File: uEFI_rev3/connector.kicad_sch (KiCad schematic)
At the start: 23 parts, among them J3 36638-0002, Q10 IRF540N, Q5 SS8050, Q6 IRF540N, Q7 IRF540N, U4 MIC2940A-3.3WU, U5 MIC2940A-5.0WT, U6 LT4363IMS

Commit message: rev3, jtag
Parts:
- U6: footprint Package_SO:SOIC-16W_7.5x10.3mm_P1.27mm -> Package_SO:MSOP-12_3x4mm_P0.65mm
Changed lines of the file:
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@@
     (property "Reference" "U6" (id 0) (at 101.6 105.029 0))
     (property "Value" "LT4363IMS" (id 1) (at 101.6 107.3404 0))
-    (property "Footprint" "Package_SO:SOIC-16W_7.5x10.3mm_P1.27mm" (id 2) (at 101.6 113.03 0)
+    (property "Footprint" "Package_SO:MSOP-12_3x4mm_P0.65mm" (id 2) (at 101.6 113.03 0)
       (effects (font (size 1.27 1.27)) hide)
     )

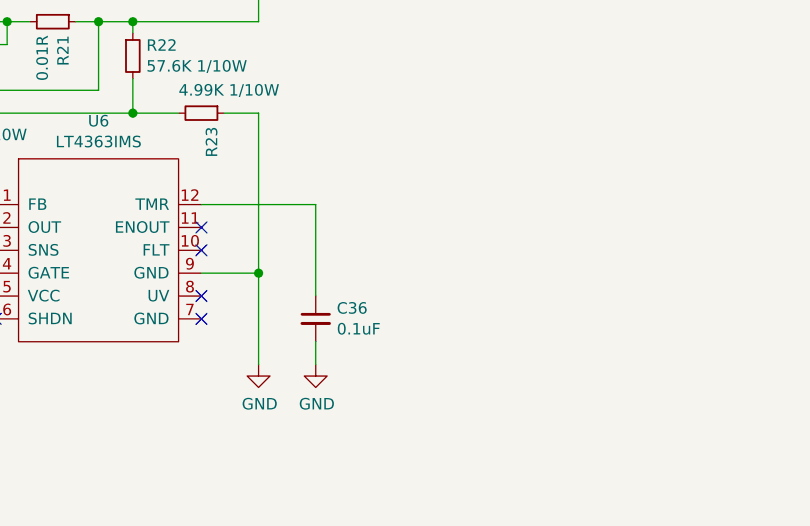
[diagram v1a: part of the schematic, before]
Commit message: fix 10k res
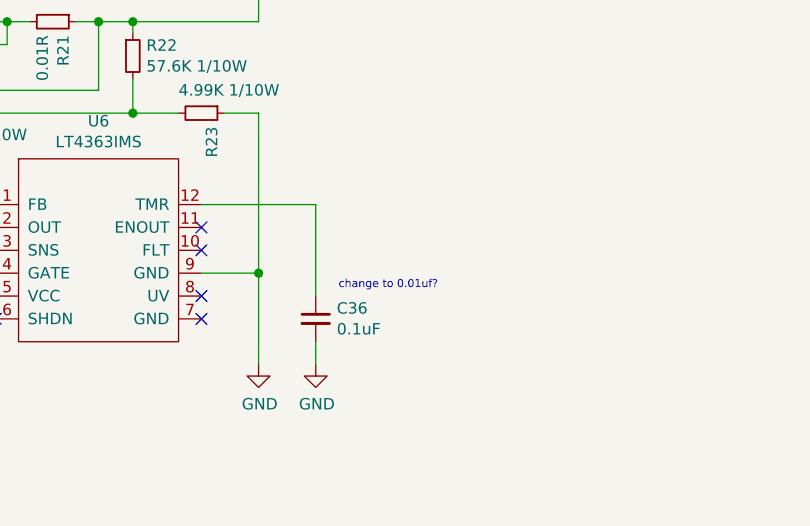
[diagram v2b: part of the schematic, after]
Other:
- note added: "change to 0.01uf?"
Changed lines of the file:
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@@
+    (effects (font (size 0.889 0.889)) (justify left bottom))
+  )
+  (text "change to 0.01uf?" (at 128.27 123.825 0)
     (effects (font (size 0.889 0.889)) (justify left bottom))
   )

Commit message: uEFI rev 3.1.0
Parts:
- removed Q6, Q7: IRF540N, Package_TO_SOT_THT:TO-220-3_Vertical, symbol Transistor_FET:IRF540N
- added Q6, Q7: IRLZ44N, Package_TO_SOT_THT:TO-220-3_Vertical, symbol Transistor_FET:IRLZ44N
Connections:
- net +12VA: now also Q6.3 (S)
- net at R21.2, U6.3 (SNS): now also Q7.3 (S)
- net at D4.1 (A1), U6.5 (VCC): now also Q6.2 (D), Q7.2 (D)
- net at R18.1: now also Q6.1 (G)
- net at R20.1: now also Q7.1 (G)
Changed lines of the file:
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@@
     (pin "9")
-  )
-  (symbol (lib_name "Transistor_FET:IRF540N_1") (lib_id "Transistor_FET:IRF540N") (at 64.77 96.52 270) (mirror x) (unit 1)
-    (in_bom yes) (on_board yes)
-    (property "Reference" "Q6" (id 0) (at 64.77 87.8332 90))
-    (property "Value" "IRF540N" (id 1) (at 64.77 90.1446 90))
-    (property "Footprint" "Package_TO_SOT_THT:TO-220-3_Vertical" (id 2) (at 62.865 90.17 0)
-      (effects (font (size 1.27 1.27) italic) (justify left) hide)
-    )
-    (property "Datasheet" "http://www.irf.com/product-info/datasheets/data/irf540n.pdf" (id 3) (at 64.77 96.52 0)
-      (effects (font (size 1.27 1.27)) (justify left) hide)
-    )
-    (pin "1")
-    (pin "2")
-    (pin "3")
-  )
-  (symbol (lib_name "Transistor_FET:IRF540N_2") (lib_id "Transistor_FET:IRF540N") (at 82.55 96.52 270) (mirror x) (unit 1)
-    (in_bom yes) (on_board yes)
-    (property "Reference" "Q7" (id 0) (at 83.7184 91.3384 0)
-      (effects (font (size 1.27 1.27)) (justify left))
-    )
-    (property "Value" "IRF540N" (id 1) (at 81.407 91.3384 0)
-      (effects (font (size 1.27 1.27)) (justify left))
-    )
-    (property "Footprint" "Package_TO_SOT_THT:TO-220-3_Vertical" (id 2) (at 80.645 90.17 0)
-      (effects (font (size 1.27 1.27) italic) (justify left) hide)
-    )
-    (property "Datasheet" "http://www.irf.com/product-info/datasheets/data/irf540n.pdf" (id 3) (at 82.55 96.52 0)
-      (effects (font (size 1.27 1.27)) (justify left) hide)
-    )
-    (pin "1")
-    (pin "2")
-    (pin "3")
   )
   (symbol (lib_id "Device:R_Small") (at 96.52 93.98 270) (unit 1)
@@
       (effects (font (size 1.27 1.27)) (justify left) hide)
     )
+    (pin "1")
+    (pin "2")
+    (pin "3")
+  )
+  (symbol (lib_id "Transistor_FET:IRLZ44N") (at 82.55 96.52 90) (unit 1)
+    (in_bom yes) (on_board yes) (fields_autoplaced)
+    (property "Reference" "Q7" (id 0) (at 82.55 86.36 90))
+    (property "Value" "IRLZ44N" (id 1) (at 82.55 88.9 90))
+    (property "Footprint" "Package_TO_SOT_THT:TO-220-3_Vertical" (id 2) (at 84.455 90.17 0)
+      (effects (font (size 1.27 1.27) italic) (justify left) hide)
+    )
+    (property "Datasheet" "http://www.irf.com/product-info/datasheets/data/irlz44n.pdf" (id 3) (at 82.55 96.52 0)
+      (effects (font (size 1.27 1.27)) (justify left) hide)
+    )
+    (pin "1")
+    (pin "2")
+    (pin "3")
+  )
+  (symbol (lib_id "Transistor_FET:IRLZ44N") (at 64.77 96.52 270) (mirror x) (unit 1)
+    (in_bom yes) (on_board yes) (fields_autoplaced)
+    (property "Reference" "Q6" (id 0) (at 64.77 86.995 90))
+    (property "Value" "IRLZ44N" (id 1) (at 64.77 89.535 90))
+    (property "Footprint" "Package_TO_SOT_THT:TO-220-3_Vertical" (id 2) (at 62.865 90.17 0)
+      (effects (font (size 1.27 1.27) italic) (justify left) hide)
+    )
+    (property "Datasheet" "http://www.irf.com/product-info/datasheets/data/irlz44n.pdf" (id 3) (at 64.77 96.52 0)
+      (effects (font (size 1.27 1.27)) (justify left) hide)
+    )

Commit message: wip v3.1
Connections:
- net 5V_ENABLE: no longer R33.1
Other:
- moved on the sheet: Q10, R33, U5

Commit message: add ckp sensor setup
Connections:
- net 5V_ENABLE: now also R33.1
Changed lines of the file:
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@@
     )
   )
-  (global_label "5V_ENABLE" (shape input) (at 114.935 57.785 0)
+  (global_label "5V_ENABLE" (shape input) (at 112.395 37.465 0)
     (effects (font (size 0.889 0.889)) (justify left))
-    (property "Intersheet References" "${INTERSHEET_REFS}" (id 0) (at 123.8207 57.7295 0)
+    (property "Intersheet References" "${INTERSHEET_REFS}" (id 0) (at 121.2807 37.4095 0)
       (effects (font (size 0.889 0.889)) (justify left) hide)
     )
